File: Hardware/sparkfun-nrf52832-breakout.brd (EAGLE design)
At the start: 17.8 x 52.1 mm, 43 parts, among them J5 CORTEX_DEBUGPTH, U1 3.3V, U2 NRF52832, Y1 32MHz, Y2 32.768kHz

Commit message: Schematic cleanup.
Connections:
- removed net N$8: J1.1
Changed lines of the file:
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@@
 <wire x1="10.5264" y1="27.94" x2="10.14" y2="27.94" width="0.1524" layer="1"/>
-</signal>
-<signal name="N$8">
-<contactref element="J1" pad="1"/>
 </signal>
 <signal name="N$14">

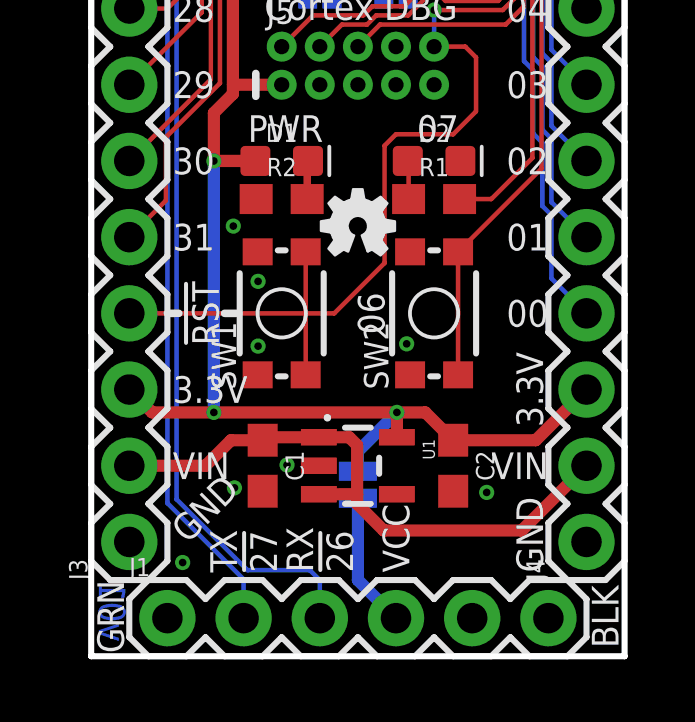
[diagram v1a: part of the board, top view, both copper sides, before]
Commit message: Adding cut-jumper to the power LED.
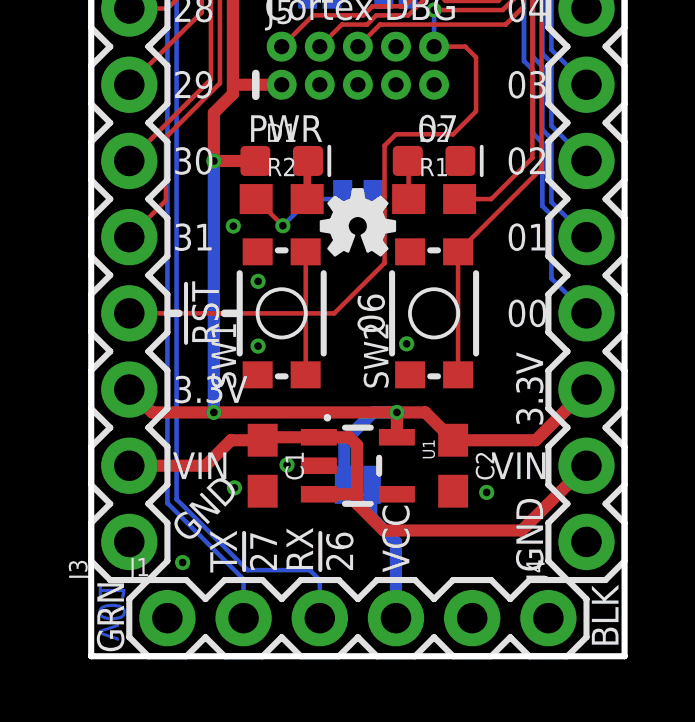
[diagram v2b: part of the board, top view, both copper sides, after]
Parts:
- added JP6: PWR-LED, SparkFun-Jumpers:PAD-JUMPER-2-NC_BY_TRACE_YES_SILK
- U1: value 3.3V -> AP2112K-3.3V
- turned JP1 to 0 degrees
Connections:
- new net N$1: JP6.2, R2.1
- net GND: now also JP6.1; no longer R2.1
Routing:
- net N$1: track 0.00 -> 3.62 mm, vias 0 -> 1
- net VDD: track 70.7 -> 71.8 mm
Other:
- board text added: "PWR-LED"
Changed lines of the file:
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@@
 <layer number="39" name="tKeepout" color="4" fill="11" visible="no" active="yes"/>
 <layer number="40" name="bKeepout" color="1" fill="11" visible="no" active="yes"/>
-<layer number="41" name="tRestrict" color="4" fill="10" visible="yes" active="yes"/>
+<layer number="41" name="tRestrict" color="4" fill="10" visible="no" active="yes"/>
 <layer number="42" name="bRestrict" color="1" fill="10" visible="no" active="yes"/>
 <layer number="43" name="vRestrict" color="2" fill="10" visible="no" active="yes"/>
@@
 <wire x1="9.2837" y1="38.8493" x2="9.3726" y2="38.8493" width="0.1524" layer="41"/>
 <wire x1="8.9027" y1="39.7383" x2="8.9916" y2="39.7383" width="0.1524" layer="41"/>
+<text x="8.8392" y="16.4338" size="0.889" layer="22" font="vector" ratio="15" rot="MR0" align="bottom-center">PWR-LED</text>
 </plain>
 <attributes>
@@
 <element name="JP4" library="SparkFun-Jumpers" package="PAD-JUMPER-2-NC_BY_TRACE_YES_SILK" value="XL1" x="7.62" y="27.94" rot="MR180"/>
 <element name="JP5" library="SparkFun-Jumpers" package="PAD-JUMPER-2-NC_BY_TRACE_YES_SILK" value="XL2" x="10.16" y="27.94" rot="MR0"/>
-<element name="U1" library="SparkFun-PowerIC" package="SOT23-5" value="3.3V" x="8.89" y="6.35" rot="R270">
+<element name="U1" library="SparkFun-PowerIC" package="SOT23-5" value="AP2112K-3.3V" x="8.89" y="6.35" rot="R270">
 <attribute name="PROD_ID" value="VREG-12457" x="8.89" y="6.35" size="1.778" layer="27" font="vector" ratio="15" rot="R270" display="off"/>
 </element>
@@
 </element>
 <element name="J1" library="SparkFun-Connectors" package="1X06" value="" x="2.54" y="1.27"/>
-<element name="JP1" library="SparkFun-Jumpers" package="PAD-JUMPER-2-NO_YES_SILK" value="VDD-EN" x="8.89" y="5.715" rot="MR90"/>
+<element name="JP1" library="SparkFun-Jumpers" package="PAD-JUMPER-2-NO_YES_SILK" value="VDD-EN" x="8.89" y="5.715" rot="MR0"/>
 <element name="J5" library="Pete_Connectors_Retired" package="2X5-PTH-1.27MM" value="CORTEX_DEBUGPTH" x="8.89" y="19.685"/>
 <element name="SW1" library="SparkFun-Electromechanical" package="TACTILE_SWITCH_SMD_4.6X2.8MM" value="" x="6.35" y="11.43" rot="R90">
@@
 <element name="JP3" library="SparkFun-Jumpers" package="SMT-JUMPER_2_NO_SILK" value="NFC2" x="10.16" y="22.225" rot="MR0"/>
 <element name="LOGO3" library="SparkFun-Aesthetics" package="SFE_LOGO_NAME_.1" value="SFE_LOGO_NAME.1_INCH" x="14.859" y="48.26" rot="MR0"/>
+<element name="JP6" library="SparkFun-Jumpers" package="PAD-JUMPER-2-NC_BY_TRACE_YES_SILK" value="PWR-LED" x="8.89" y="15.24" rot="MR0"/>
 </elements>
 <signals>
@@
 <contactref element="J5" pad="3"/>
 <contactref element="J5" pad="5"/>
-<contactref element="R2" pad="1"/>
 <via x="4.7371" y="14.3383" extent="1-16" drill="0.254"/>
 <via x="5.5626" y="12.4968" extent="1-16" drill="0.254"/>
@@
 <via x="13.589" y="45.339" extent="1-16" drill="0.254"/>
 <via x="14.859" y="45.339" extent="1-16" drill="0.254"/>
+<contactref element="JP6" pad="1"/>
 </signal>
 <signal name="P00">
@@
 <wire x1="5.6134" y1="32.0294" x2="5.6134" y2="27.94" width="0.4064" layer="16"/>
 <wire x1="5.6134" y1="27.94" x2="5.08" y2="27.4066" width="0.4064" layer="16"/>
-<wire x1="10.16" y1="8.0979" x2="10.1901" y2="8.128" width="0.4064" layer="16"/>
 <via x="10.1901" y="8.128" extent="1-16" drill="0.254"/>
 <contactref element="J5" pad="1"/>
@@
 <wire x1="6.35" y1="19.05" x2="4.7244" y2="19.05" width="0.4064" layer="1"/>
 <wire x1="4.0894" y1="16.51" x2="5.473" y2="16.51" width="0.4064" layer="1"/>
-<wire x1="8.89" y1="6.165" x2="8.89" y2="6.8279" width="0.4064" layer="16"/>
-<wire x1="8.89" y1="6.8279" x2="10.1901" y2="8.128" width="0.4064" layer="16"/>
 <via x="5.8674" y="38.8874" extent="1-16" drill="0.254"/>
 <wire x1="7.239" y1="38.8874" x2="5.8674" y2="38.8874" width="0.2286" layer="1"/>
 <wire x1="5.842" y1="36.4744" x2="5.8674" y2="36.4998" width="0.2286" layer="16"/>
 <wire x1="5.8674" y1="36.4998" x2="5.8674" y2="38.8874" width="0.2286" layer="16"/>
+<wire x1="8.44" y1="5.715" x2="8.44" y2="7.17" width="0.4064" layer="16"/>
+<wire x1="10.1901" y1="8.128" x2="9.398" y2="8.128" width="0.4064" layer="16"/>
+<wire x1="9.398" y1="8.128" x2="8.44" y2="7.17" width="0.4064" layer="16"/>
 </signal>
 <signal name="DEC1">
@@
 <contactref element="J1" pad="4"/>
 <contactref element="JP1" pad="1"/>
-<wire x1="10.16" y1="1.27" x2="8.89" y2="2.54" width="0.4064" layer="16"/>
-<wire x1="8.89" y1="2.54" x2="8.89" y2="5.265" width="0.4064" layer="16"/>
+<wire x1="9.34" y1="5.715" x2="9.34" y2="4.63" width="0.4064" layer="16"/>
+<wire x1="9.34" y1="4.63" x2="10.16" y2="3.81" width="0.4064" layer="16"/>
+<wire x1="10.16" y1="3.81" x2="10.16" y2="1.27" width="0.4064" layer="16"/>
 </signal>
 <signal name="VIN">
@@
 <wire x1="10.5664" y1="22.225" x2="11.049" y2="22.225" width="0.1524" layer="16"/>
 </signal>
+<signal name="N$1">
+<contactref element="R2" pad="1"/>
+<contactref element="JP6" pad="2"/>
+<wire x1="5.5" y1="15.24" x2="6.389" y2="14.351" width="0.1524" layer="1"/>
+<via x="6.389" y="14.351" extent="1-16" drill="0.254"/>
+<wire x1="6.389" y1="14.351" x2="7.278" y2="15.24" width="0.1524" layer="16"/>
+<wire x1="7.278" y1="15.24" x2="8.382" y2="15.24" width="0.1524" layer="16"/>
+</signal>
 </signals>

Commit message: Updates after running checklist.
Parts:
- added FD1, FD2: FIDUCIAL1X2, SparkFun-Aesthetics:FIDUCIAL-1X2
- moved C12 0.13 mm to (9.53, 44.5)
- moved C10 0.10 mm to (4.45, 39.5)
- moved C5 0.10 mm to (6.50, 41.9)
- moved L1 0.07 mm to (10.1, 42.5)
- moved C14 0.05 mm to (10.6, 29.8)
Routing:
- net GND: vias 63 -> 61
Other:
- board text added: "00 !XL1"
- board text added: "00 !XL1!"
- board text added: "01 !XL2"
- board text added: "02 !A0"
- board text added: "03 !A1"
- board text added: "04 !A2"
- board text added: "05 !A3"
- board text added: "09 !NFC1"
- board text added: "10 !NFC2"
- board text added: "26 !RX"
- board text added: "27 !TX"
- board text added: "28 !A4"
- board text added: "29 !A5"
- board text added: "30 !A6"
- board text added: "31 !A7"
- board text added: "Units in inches"
- board text removed: "00"
- board text removed: "01"
- board text removed: "02"
- board text removed: "03"
- board text removed: "04"
- board text removed: "05"
- board text removed: "28"
- board text removed: "29"
- board text removed: "30"
- board text removed: "31"
- board text removed: "RX !26!"
- board text removed: "TX !27!"

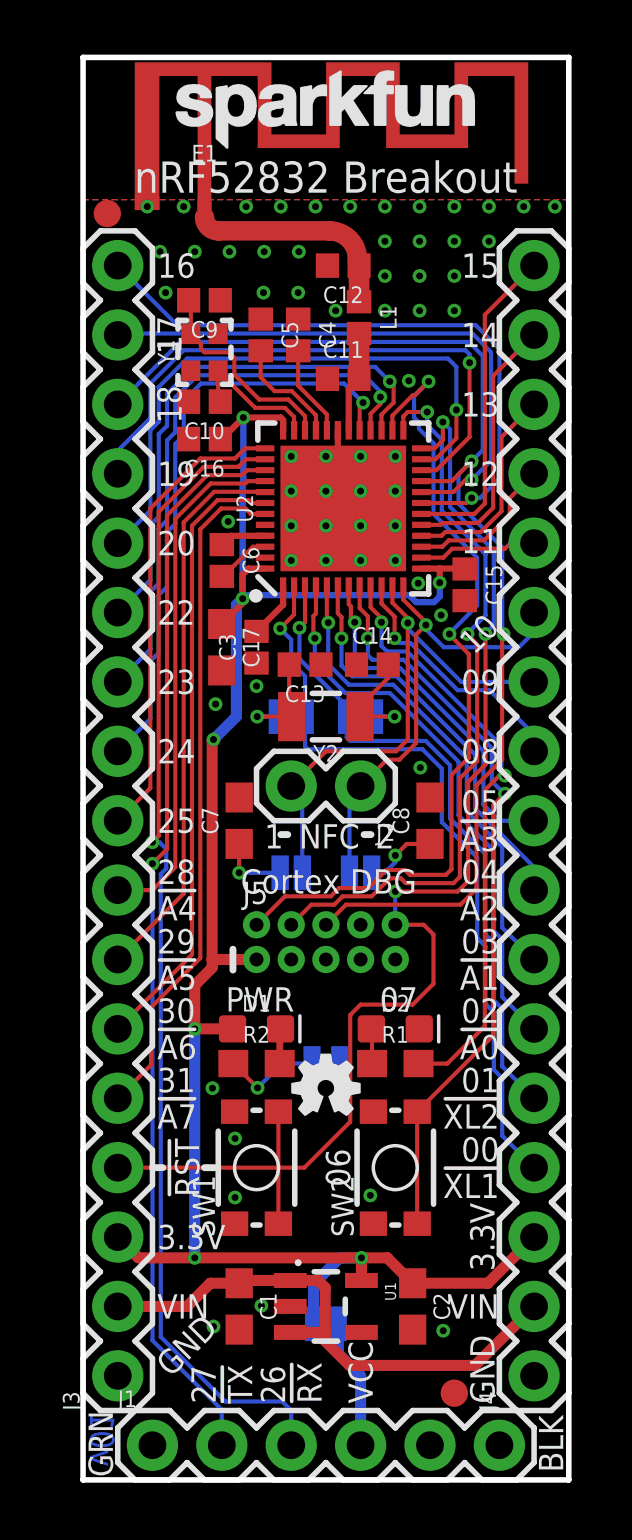
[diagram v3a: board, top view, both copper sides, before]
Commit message: Adding test points to swd pins, stubs to NC QFN pins.
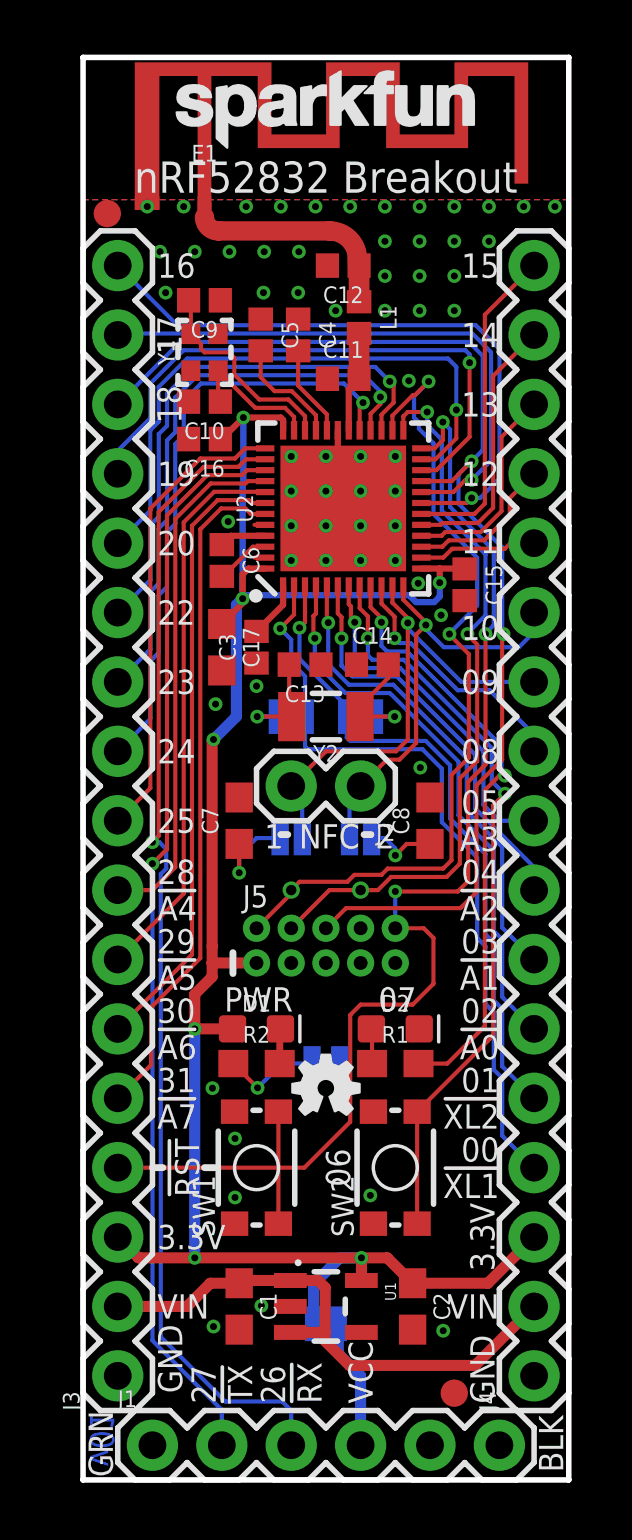
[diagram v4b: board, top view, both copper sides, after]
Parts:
- added TP1, TP2: (no value), SparkFun-Connectors:TP_15TH
- moved JP2 1.27 mm to (7.62, 23.5)
- moved JP3 1.27 mm to (10.2, 23.5)
- moved J5 0.13 mm to (8.89, 19.6)
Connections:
- new net DCC: U2.47
- new net NC: U2.44
- net SWDCLK: now also TP2.P$1
- net SWDIO: now also TP1.P$1
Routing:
- net P10: track 17.7 -> 16.4 mm
- net P09: track 19.8 -> 18.5 mm
- net NFC1: track 2.85 -> 3.75 mm
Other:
- board text removed: "Cortex DBG"
- board text removed: "NFC-EN"

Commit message: Moving test points to bottom, switching to micro fids, silk nudging.
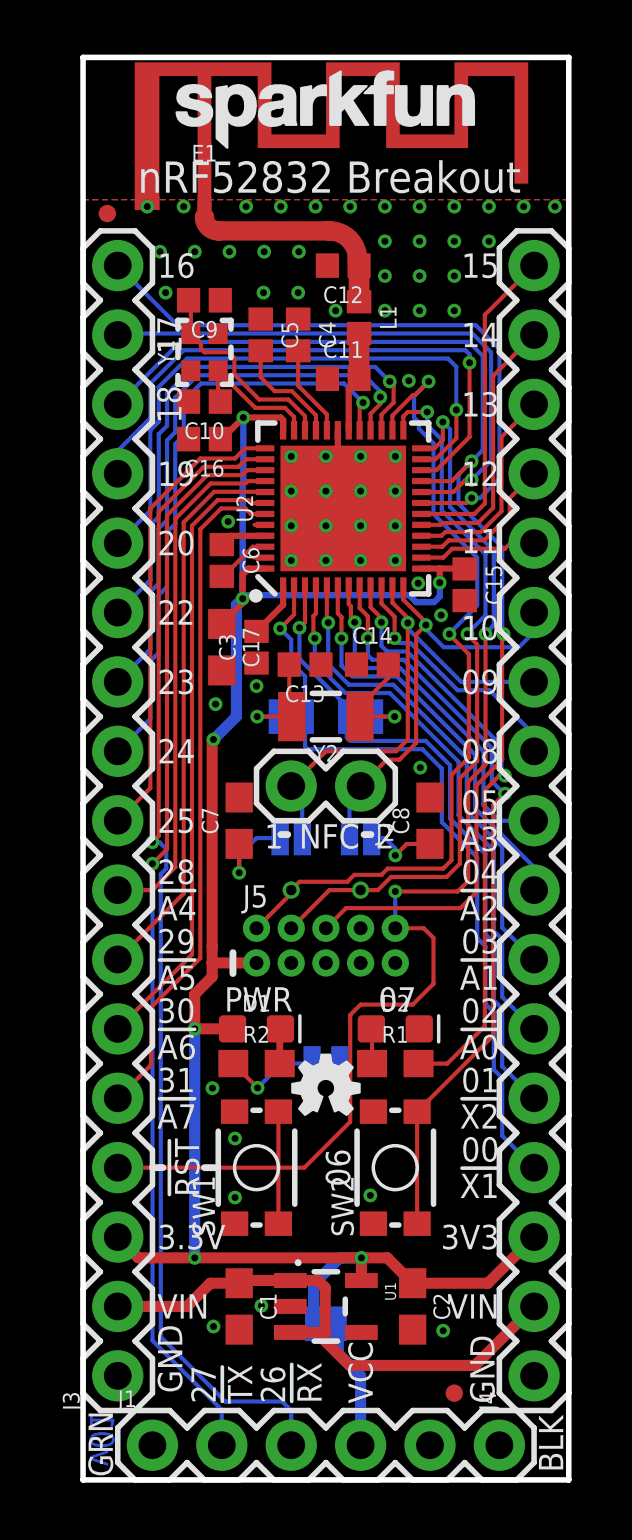
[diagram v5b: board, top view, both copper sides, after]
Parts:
- FD1, FD2: value FIDUCIAL1X2 -> FIDUCIALUFIDUCIAL; device SparkFun-Aesthetics:FIDUCIAL-1X2 -> SparkFun-Aesthetics:FIDUCIAL-MICRO
- flipped TP1 to the top
- flipped TP2 to the top
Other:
- board text added: "00 !X1"
- board text added: "01 !X2"
- board text added: "3V3"
- board text removed: "00 !XL1"
- board text removed: "00 !XL1!"
- board text removed: "01 !XL2"
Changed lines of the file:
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@@
 <setting verticaltext="up"/>
 </settings>
-<grid distance="0.001" unitdist="inch" unit="inch" style="lines" multiple="1" display="yes" altdistance="0.0005" altunitdist="inch" altunit="inch"/>
+<grid distance="0.05" unitdist="inch" unit="inch" style="lines" multiple="1" display="yes" altdistance="0.005" altunitdist="inch" altunit="inch"/>
 <layers>
 <layer number="1" name="Top" color="4" fill="1" visible="yes" active="yes"/>
@@
 !A0</text>
 <text x="15.24" y="13.97" size="0.889" layer="21" font="vector" ratio="15" align="center-right">01
-!XL2</text>
+!X2</text>
 <text x="15.24" y="11.43" size="0.889" layer="21" font="vector" ratio="15" align="center-right">00
-!XL1</text>
+!X1</text>
 <text x="15.24" y="6.35" size="0.889" layer="21" font="vector" ratio="15" align="center-right">VIN</text>
 <text x="2.7178" y="41.91" size="0.889" layer="21" font="vector" ratio="15" rot="R270" align="bottom-center">17</text>
@@
 <text x="14.6177" y="2.794" size="0.889" layer="21" font="vector" ratio="15" rot="R90" align="center-left">GND</text>
 <text x="10.16" y="2.794" size="0.889" layer="21" font="vector" ratio="15" rot="R90" align="center-left">VCC</text>
-<text x="8.89" y="48.26" size="1.143" layer="21" font="vector" ratio="15" align="top-center">nRF52832 Breakout</text>
+<text x="9.017" y="48.26" size="1.143" layer="21" font="vector" ratio="15" align="top-center">nRF52832 Breakout</text>
 <text x="2.413" y="44.45" size="0.889" layer="22" font="vector" ratio="15" rot="MR0" align="center-right">16</text>
 <text x="2.413" y="41.91" size="0.889" layer="22" font="vector" ratio="15" rot="MR0" align="center-right">17</text>
@@
 !A0</text>
 <text x="15.113" y="13.97" size="0.889" layer="22" font="vector" ratio="15" rot="MR0" align="center-left">01
-!XL2</text>
+!X2</text>
 <text x="15.113" y="11.43" size="0.889" layer="22" font="vector" ratio="15" rot="MR0" align="center-left">00
-!XL1!</text>
+!X1</text>
 <text x="15.113" y="8.89" size="0.889" layer="22" font="vector" ratio="15" rot="MR0" align="center-left">3.3V</text>
 <text x="15.113" y="6.35" size="0.889" layer="22" font="vector" ratio="15" rot="MR0" align="center-left">VIN</text>
@@
 <text x="11.049" y="25.4" size="1.143" layer="22" font="vector" ratio="15" rot="MR0" align="center-right">2</text>
 <text x="8.89" y="29.1338" size="0.889" layer="22" font="vector" ratio="15" rot="MR0" align="bottom-center">RTC-EN</text>
-<text x="8.89" y="48.26" size="1.143" layer="22" font="vector" ratio="15" rot="MR0" align="top-center">nRF52832 Breakout</text>
+<text x="8.763" y="48.26" size="1.143" layer="22" font="vector" ratio="15" rot="MR0" align="top-center">nRF52832 Breakout</text>
 <text x="1.143" y="1.4986" size="0.889" layer="16" font="vector" ratio="20" rot="MR270" align="bottom-center">v01</text>
 <text x="8.89" y="45.466" size="0.889" layer="22" font="vector" ratio="15" rot="MR0" align="bottom-center">http://sfe.io/t549</text>
@@
 <text x="6.4262" y="17.145" size="0.889" layer="21" font="vector" ratio="15" align="bottom-center">PWR</text>
 <text x="11.5062" y="17.145" size="0.889" layer="21" font="vector" ratio="15" align="bottom-center">07</text>
-<text x="15.0622" y="8.89" size="0.889" layer="21" font="vector" ratio="15" rot="R90" align="bottom-center">3.3V</text>
 <wire x1="7.239" y1="23.622" x2="7.493" y2="23.622" width="0.254" layer="21"/>
 <wire x1="10.287" y1="23.622" x2="10.541" y2="23.622" width="0.254" layer="21"/>
@@
 <text x="3.1877" y="3.175" size="0.889" layer="21" font="vector" ratio="15" rot="R90" align="center-left">GND</text>
 <text x="3.1623" y="3.175" size="0.889" layer="22" font="vector" ratio="15" rot="MR90" align="center-left">GND</text>
+<text x="15.24" y="8.89" size="0.889" layer="21" font="vector" ratio="15" align="center-right">3V3</text>
 </plain>
 <attributes>
@@
 <element name="LOGO3" library="SparkFun-Aesthetics" package="SFE_LOGO_NAME_.1" value="SFE_LOGO_NAME.1_INCH" x="14.859" y="48.26" rot="MR0"/>
 <element name="JP6" library="SparkFun-Jumpers" package="PAD-JUMPER-2-NC_BY_TRACE_YES_SILK" value="PWR-LED" x="8.89" y="15.24" rot="MR0"/>
-<element name="FD1" library="SparkFun-Aesthetics" package="FIDUCIAL-1X2" value="FIDUCIAL1X2" x="13.589" y="3.175"/>
-<element name="FD2" library="SparkFun-Aesthetics" package="FIDUCIAL-1X2" value="FIDUCIAL1X2" x="0.889" y="46.355"/>
-<element name="TP1" library="SparkFun-Connectors" package="TP_15TH" value="" x="7.62" y="21.59" rot="MR0"/>
-<element name="TP2" library="SparkFun-Connectors" package="TP_15TH" value="" x="10.16" y="21.59" rot="MR0"/>
+<element name="FD1" library="SparkFun-Aesthetics" package="FIDUCIAL-MICRO" value="FIDUCIALUFIDUCIAL" x="13.589" y="3.175"/>
+<element name="FD2" library="SparkFun-Aesthetics" package="FIDUCIAL-MICRO" value="FIDUCIALUFIDUCIAL" x="0.889" y="46.355"/>
+<element name="TP1" library="SparkFun-Connectors" package="TP_15TH" value="" x="7.62" y="21.59"/>
+<element name="TP2" library="SparkFun-Connectors" package="TP_15TH" value="" x="10.16" y="21.59"/>
 </elements>
 <signals>
